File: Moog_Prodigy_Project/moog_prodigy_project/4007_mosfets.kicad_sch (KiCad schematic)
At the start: 49 parts, among them Q20 BC327, Q21 BC327, SW12 FINAL DECAY SWITCH, SW13 FINAL DECAY SWITCH, U20 NE556N, U21 MC14007UBCP, U22 MC14007UBCP, U23 MC14007UBCP, U26 OPA184, U27 OPA184

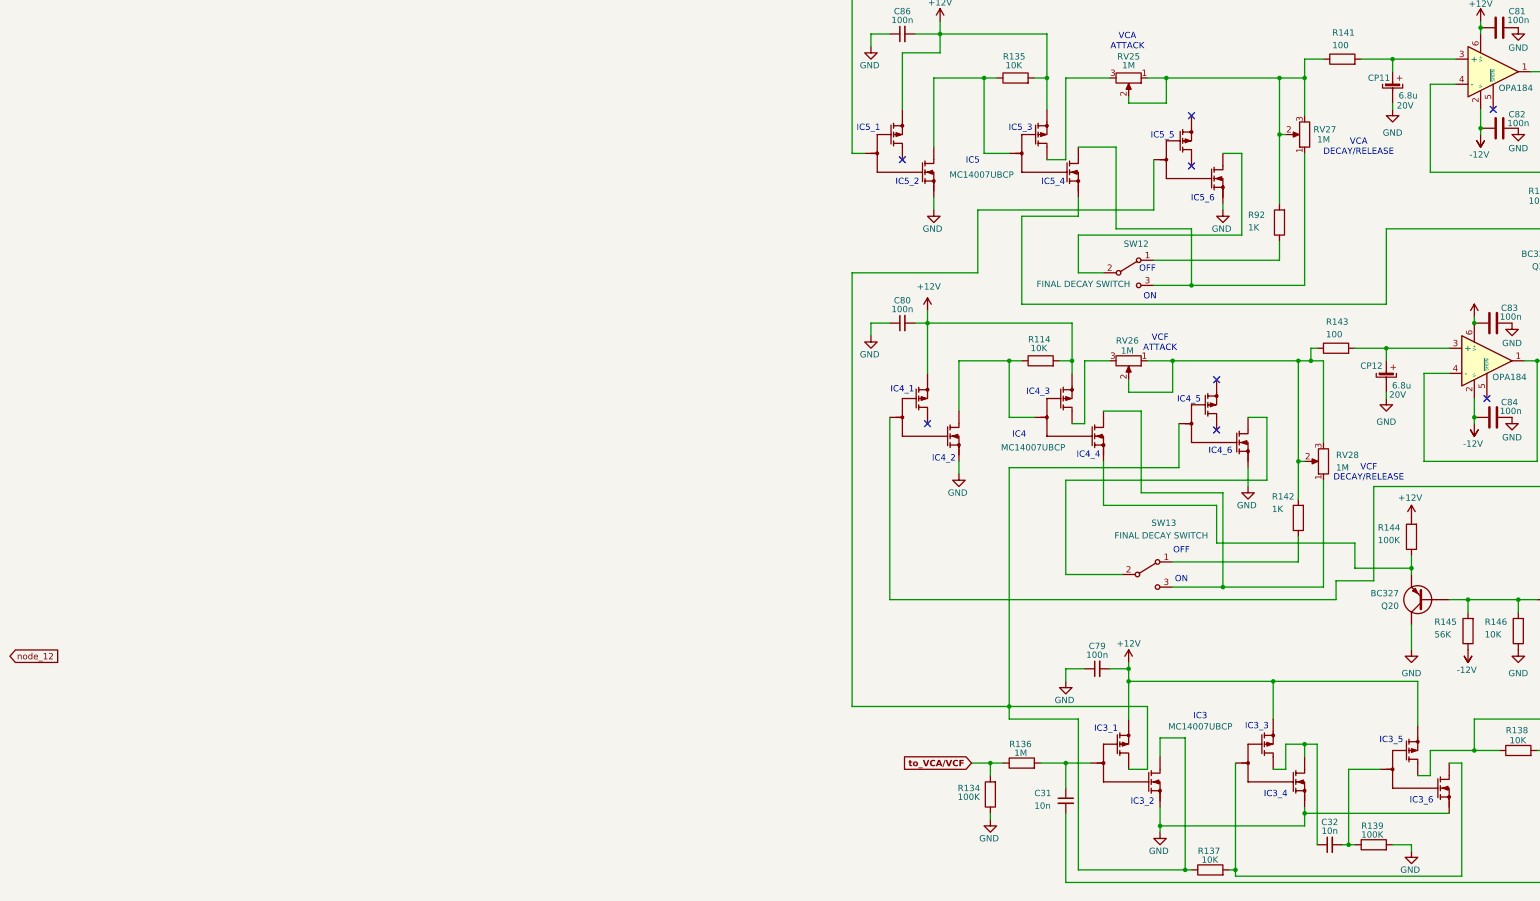
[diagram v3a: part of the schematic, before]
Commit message: Moog prodigy fix 3
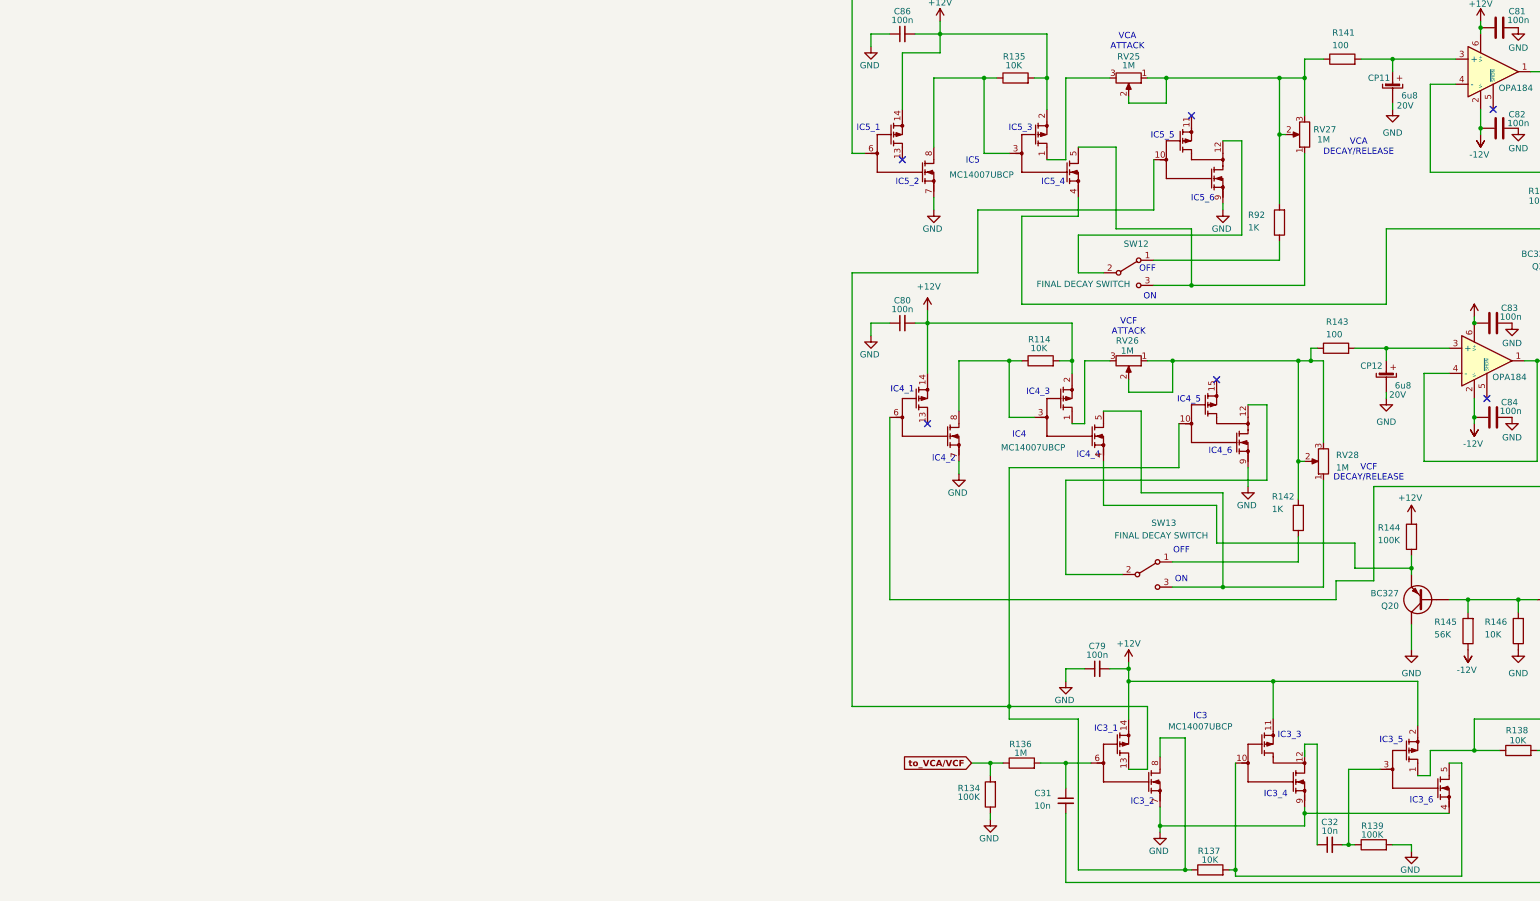
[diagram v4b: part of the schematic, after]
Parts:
- CP11, CP12: value 6.8u -> 6u8
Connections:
- net +12V: now also U21.14, U21.2, U22.11, U22.14, U22.2, U23.14, U23.2; no longer U21., U22., U23.
- net GND: now also U21.7, U21.9, U22.4, U22.7, U22.9, U23.7, U23.9; no longer U21., U22., U23.
- net TRIGGER: now also U22.1; no longer U22.
- net at C32.2, R139.1: now also U22.3; no longer U22.
- net at R137.2: now also U22.10, U22.5; no longer U22.
- net at C31.1, R136.2: now also U22.6; no longer U22.
- net at C32.1: no longer U22.
- net at RV26.3: now also U23.1; no longer U23.
- net at RV27.1, SW12.3 (C): now also U21.5; no longer U21.
- net at R135.1: now also U21.3, U21.8; no longer U21.
- net at RV25.3: now also U21.1; no longer U21.
- net at U20.5 (1OUT): now also U21.6; no longer U21.
- net at SW12.2 (B): now also U21.12; no longer U21.
- net at RV28.1, SW13.3 (C): now also U23.5; no longer U23.
- net at R114.1: now also U23.3, U23.8; no longer U23.
- net at U20.9 (2OUT): now also U23.6; no longer U23.
- net at SW13.2 (B): now also U23.12; no longer U23.
- new net: Q20. (E), R144.1, U23.4
- new net: Q21. (E), R148.1, U21.4
- new net: R137.1, U21.10, U22.13, U22.8, U23.10
- no-connect marks 12 -> 10
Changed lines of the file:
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@@
 	(text "VCF\nATTACK"
 		(exclude_from_sim no)
-		(at 76.2 87.884 0)
+		(at 69.85 84.582 0)
 		(effects
 			(font
@@
 	(text "IC3_3"
 		(exclude_from_sim no)
-		(at 95.758 165.354 0)
+		(at 102.362 167.132 0)
 		(effects
 			(font
@@
 	)
 	(junction
-		(at 105.41 168.91)
-		(diameter 0)
-		(color 0 0 0 0)
-	)
-	(junction
 		(at 40.64 34.29)
 		(diameter 0)
@@
 	)
 	(no_connect
-		(at 87.63 105.41)
-	)
-	(no_connect
 		(at 254 102.87)
 	)
@@
 	)
 	(no_connect
-		(at 82.55 52.07)
-	)
-	(no_connect
 		(at 143.51 40.64)
 	)
@@
 	(wire
 		(pts
-			(xy 101.6 168.91) (xy 105.41 168.91)
-		)
-		(stroke
-			(width 0)
-			(type default)
-		)
-	)
-	(wire
-		(pts
 			(xy 115.57 133.35) (xy 127 133.35)
 		)
@@
 	(wire
 		(pts
-			(xy 88.9 49.53) (xy 92.71 49.53)
+			(xy 88.9 46.99) (xy 92.71 46.99)
 		)
 		(stroke
@@
 	(wire
 		(pts
-			(xy 101.6 173.99) (xy 101.6 168.91)
-		)
-		(stroke
-			(width 0)
-			(type default)
-		)
-	)
-	(wire
-		(pts
 			(xy 209.55 118.11) (xy 209.55 114.3)
 		)
@@
 	(wire
 		(pts
-			(xy 97.79 102.87) (xy 97.79 115.57)
+			(xy 97.79 100.33) (xy 97.79 115.57)
 		)
 		(stroke
@@
 	(wire
 		(pts
-			(xy 99.06 173.99) (xy 101.6 173.99)
-		)
-		(stroke
-			(width 0)
-			(type default)
-		)
-	)
-	(wire
-		(pts
 			(xy 123.19 30.48) (xy 135.89 30.48)
 		)
@@
 	(wire
 		(pts
-			(xy 93.98 102.87) (xy 97.79 102.87)
+			(xy 93.98 100.33) (xy 97.79 100.33)
 		)
 		(stroke
@@
 	(wire
 		(pts
-			(xy 92.71 49.53) (xy 92.71 66.04)
+			(xy 92.71 46.99) (xy 92.71 66.04)
 		)
 		(stroke
@@
 		)
 	)
-	(global_label "node_12"
-		(shape input)
-		(at -156.21 151.13 0)
-		(fields_autoplaced yes)
-		(effects
-			(font
-				(size 1.27 1.27)
-			)
-			(justify left)
-		)
-		(property "Intersheetrefs" "${INTERSHEET_REFS}"
-			(at -145.3026 151.13 0)
-			(effects
-				(font
-					(size 1.27 1.27)
-				)
-				(justify left)
-				(hide yes)
-			)
-		)
-	)
 	(symbol
 		(lib_id "Device:R")
@@
 			)
 		)
-		(property "Value" "6.8u"
+		(property "Value" "6u8"
 			(at 128.27 37.846 0)
 			(effects
@@
 			)
 		)
-		(pin ""
-		)
-		(pin ""
+		(pin "11"
 		)
-		(pin ""
+		(pin "2"
 		)
-		(pin ""
+		(pin "1"
 		)
-		(pin ""
+		(pin "12"
 		)
-		(pin ""
+		(pin "6"
 		)
-		(pin ""
+		(pin "10"
 		)
-		(pin ""
+		(pin "14"
 		)
-		(pin ""
+		(pin "13"
 		)
-		(pin ""
+		(pin "7"
 		)
-		(pin ""
+		(pin "8"
 		)
-		(pin ""
+		(pin "5"
 		)
-		(pin ""
+		(pin "4"
 		)
-		(pin ""
+		(pin "3"
 		)
-		(pin ""
+		(pin "9"
 		)
 		(instances
@@
 			)
 		)
-		(property "Value" "6.8u"
+		(property "Value" "6u8"
 			(at 126.9492 96.4438 0)
 			(effects
@@
 			)
 		)
-		(pin ""
-		)
-		(pin ""
+		(pin "6"
 		)
-		(pin ""
+		(pin "5"
 		)
-		(pin ""
+		(pin "13"
 		)
-		(pin ""
+		(pin "1"
 		)
-		(pin ""
+		(pin "2"
 		)
-		(pin ""
+		(pin "8"
 		)
-		(pin ""
+		(pin "3"
 		)
-		(pin ""
+		(pin "11"
 		)
-		(pin ""
+		(pin "10"
 		)
-		(pin ""
+		(pin "7"
 		)
-		(pin ""
+		(pin "4"
 		)
-		(pin ""
+		(pin "9"
 		)
-		(pin ""
+		(pin "12"
 		)
-		(pin ""
+		(pin "14"
 		)
 		(instances
@@
 			)
 		)
-		(pin ""
+		(pin "3"
 		)
-		(pin ""
+		(pin "15"
 		)
-		(pin ""
+		(pin "10"
 		)
-		(pin ""
+		(pin "14"
 		)
-		(pin ""
+		(pin "9"
 		)
-		(pin ""
+		(pin "7"
 		)
-		(pin ""
+		(pin "4"
 		)
-		(pin ""
+		(pin "12"
 		)
-		(pin ""
+		(pin "13"
 		)
-		(pin ""
-		)
-		(pin ""
+		(pin "5"
 		)
-		(pin ""
+		(pin "8"
 		)
-		(pin ""
+		(pin "6"
 		)
-		(pin ""
+		(pin "2"
 		)
-		(pin ""
+		(pin "1"
 		)
 		(instances
